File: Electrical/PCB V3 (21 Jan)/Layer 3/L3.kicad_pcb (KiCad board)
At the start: 2 copper layers, 117.9 x 110 mm, 28 parts, among them J1 Conn_01x06, J2 Conn_02x08_Odd_Even, J3 Conn_01x06, J4 Conn_01x06, J5 Conn_01x06, U2 113991054, U3 4754

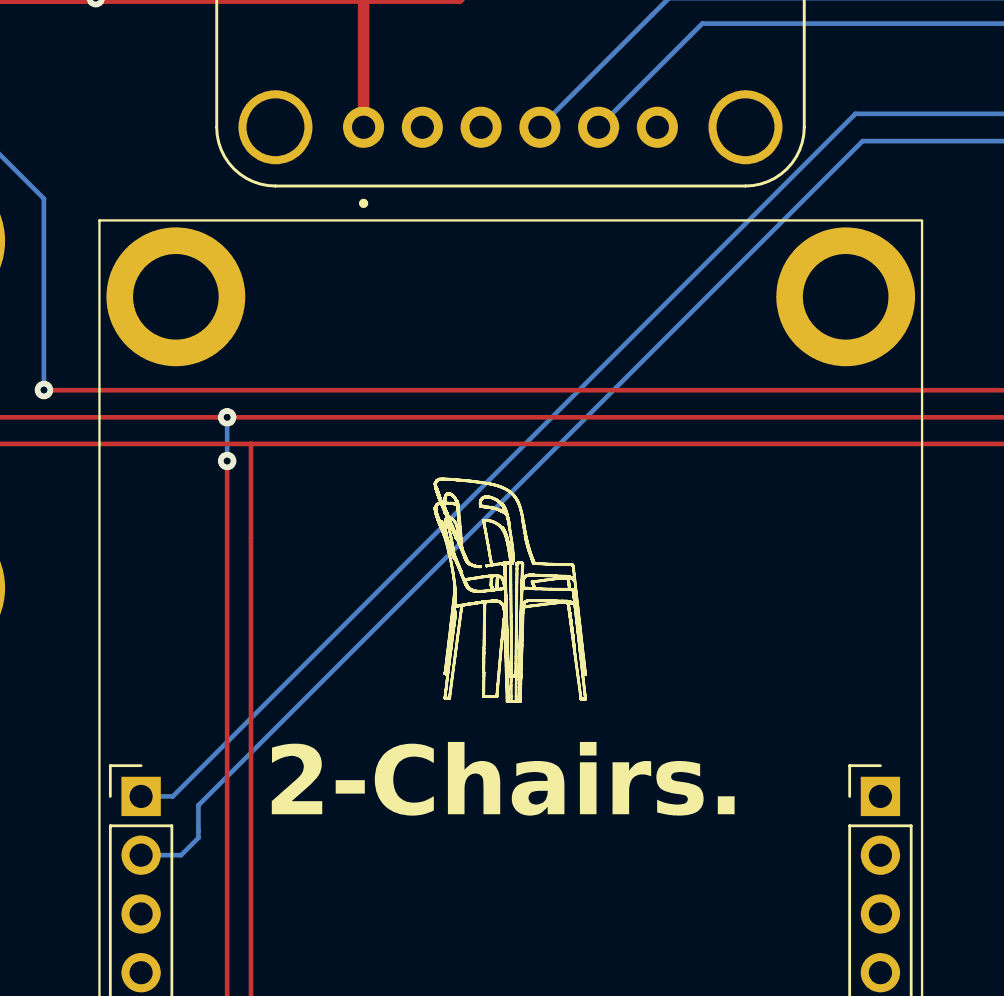
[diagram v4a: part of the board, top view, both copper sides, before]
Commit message: change l3 files to kicad 9, made ONE trace look nicer
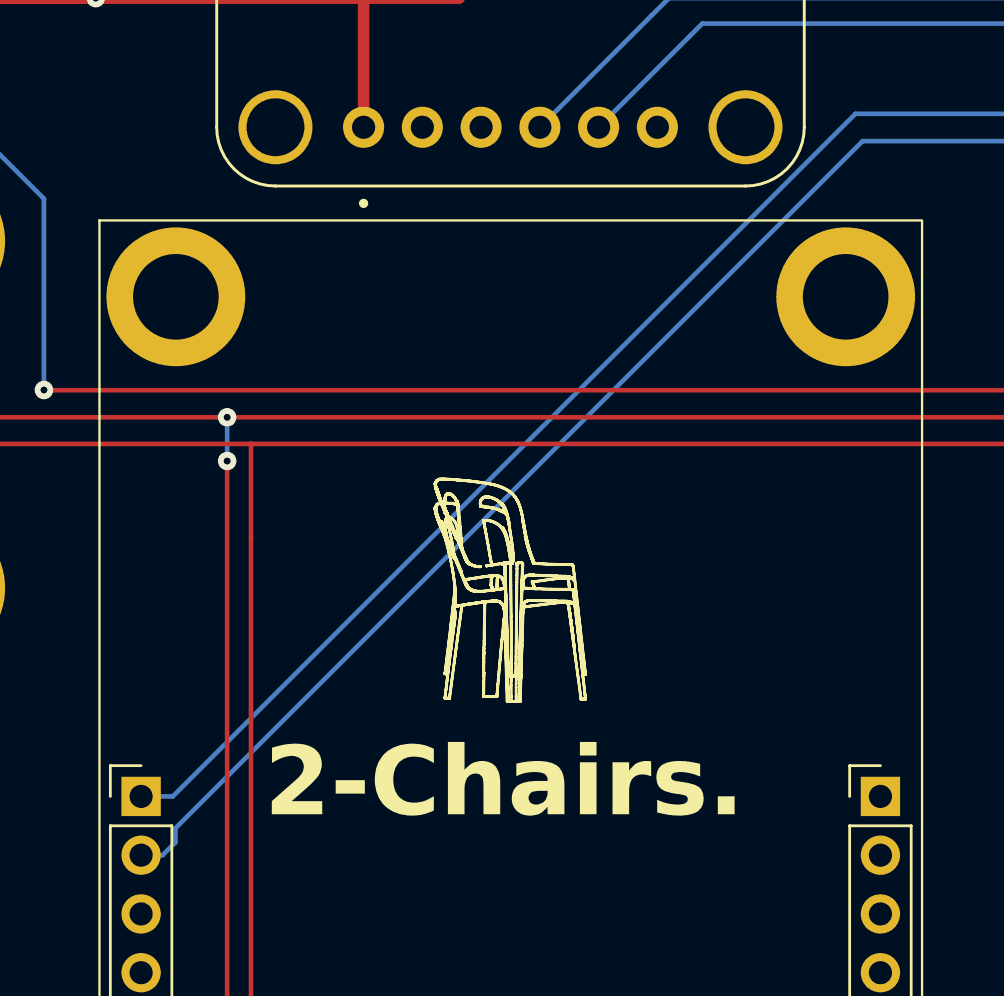
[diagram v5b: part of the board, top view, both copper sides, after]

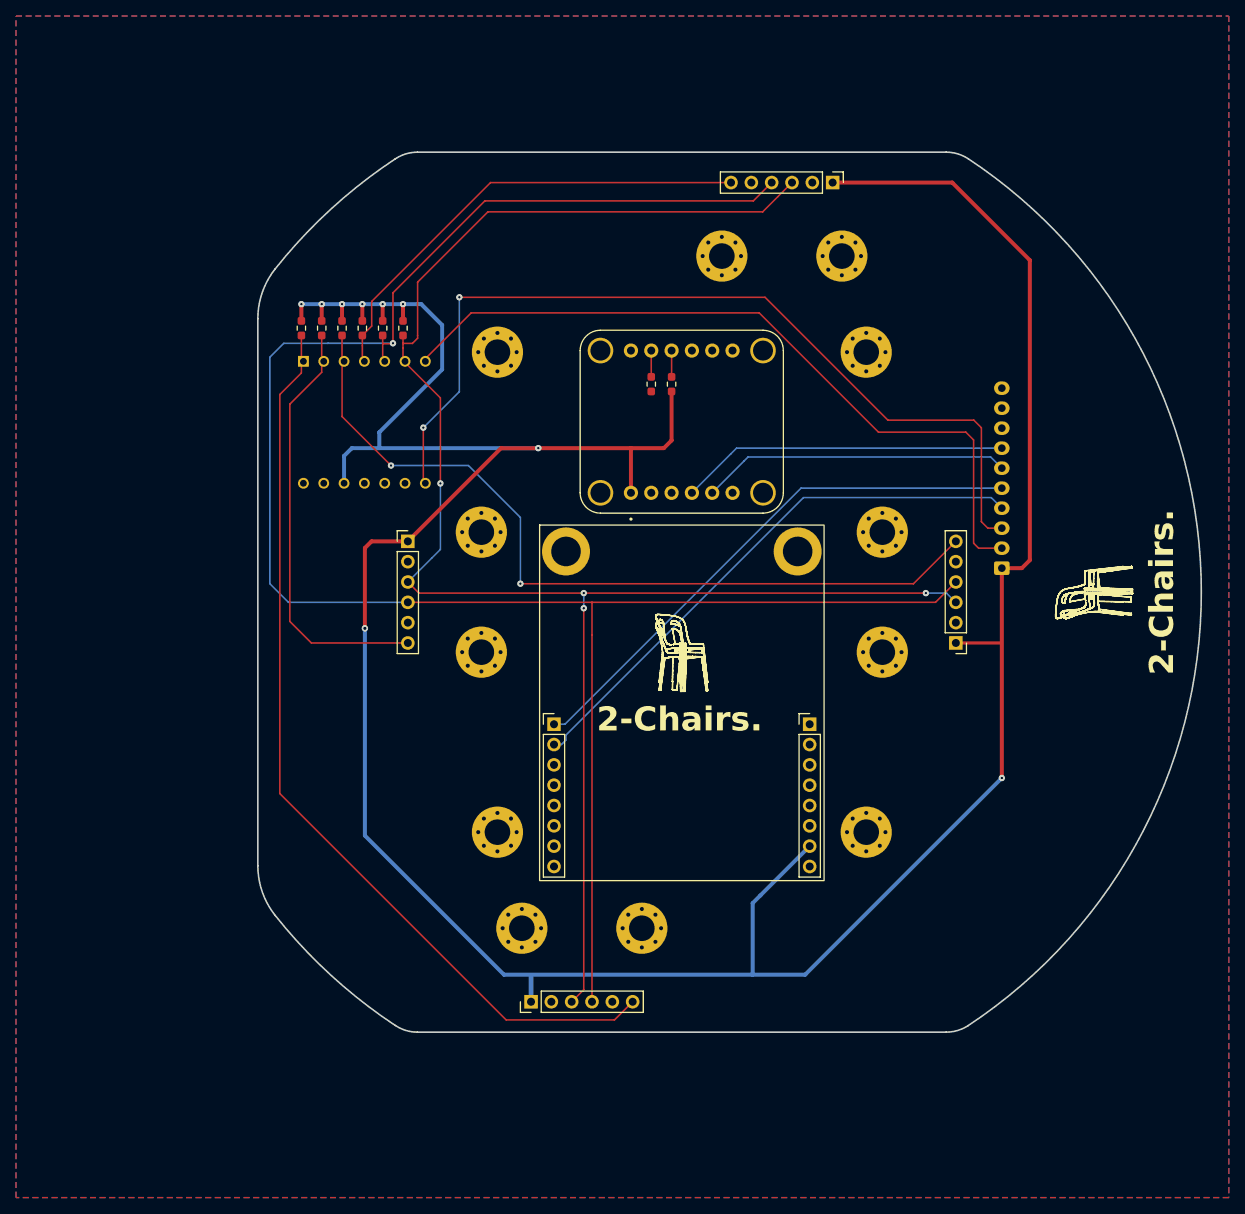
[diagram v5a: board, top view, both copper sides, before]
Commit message: fixed l1 and l3
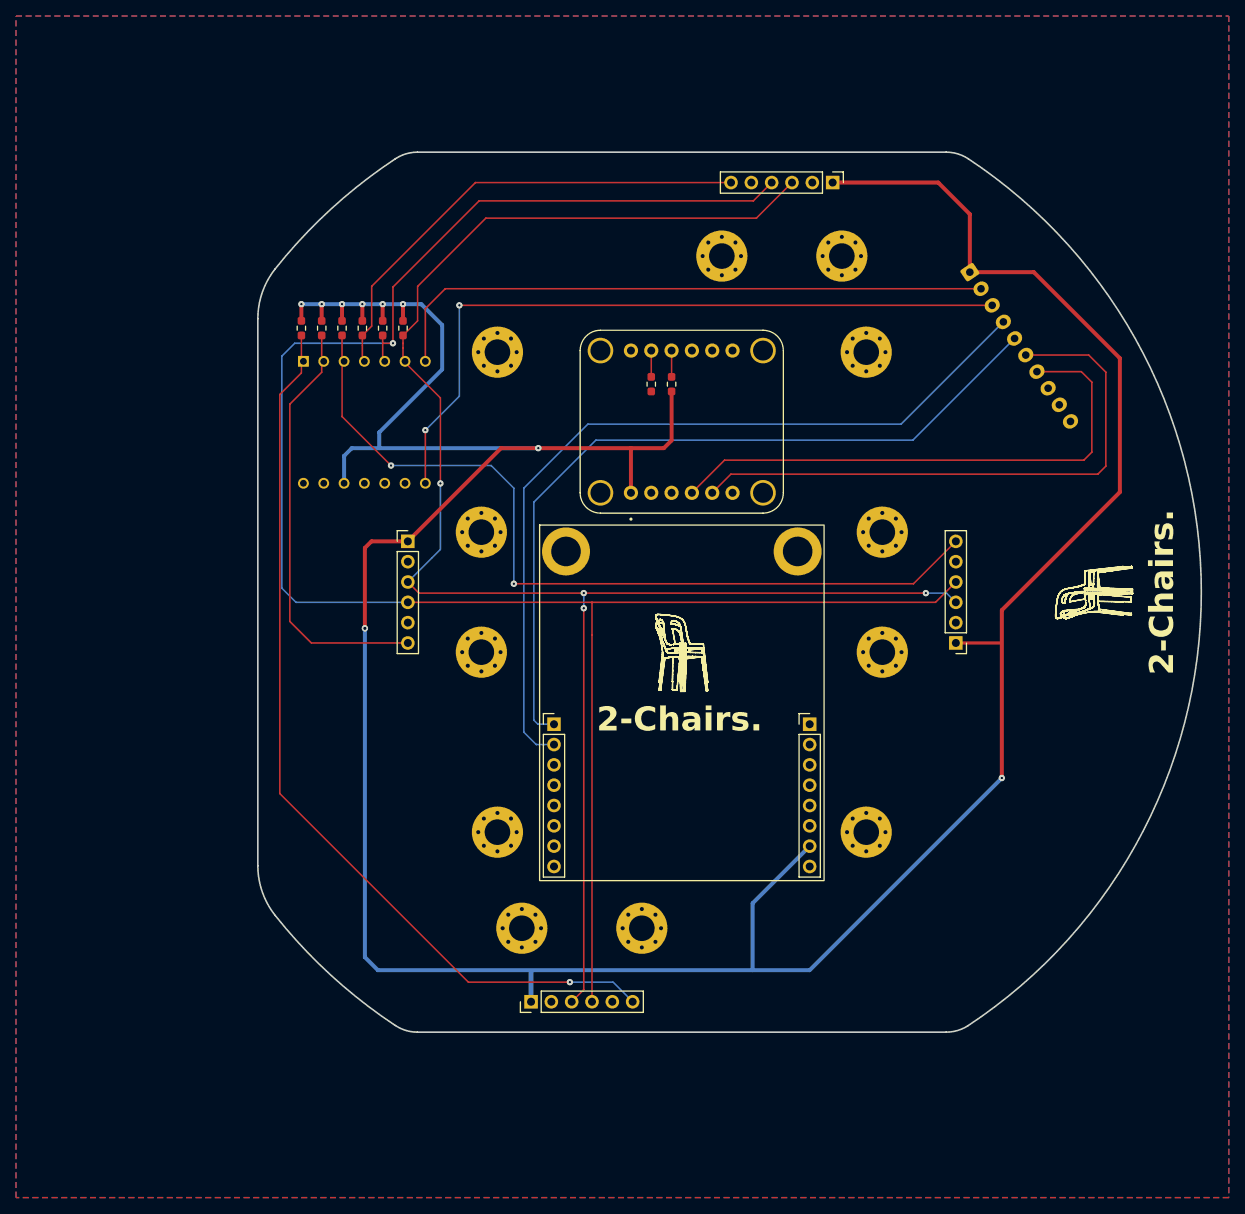
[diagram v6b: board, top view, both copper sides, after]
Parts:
- moved J2 37.2 mm to (249.7, 47.5), turned to -56 degrees
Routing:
- net /TX (IMU): track 38.6 -> 73.2 mm
- net /TX (CAM): track 70.2 -> 104.0 mm
- net /RX (CAM): track 68.2 -> 98.5 mm
- net /RX (IMU): track 41.1 -> 68.3 mm
- net /RX (L3 ESP32): track 111.7 -> 90.6 mm
- net +3V3: track 390.8 -> 410.7 mm
- net /TX (L3 ESP32): track 94.5 -> 77.1 mm
- net /SDA: track 245.9 -> 243.7 mm
- net /TOF3 XSHUT: track 102.6 -> 104.7 mm
- net /SCL: track 216.8 -> 214.8 mm
- net /TOF1 XSHUT: track 115.1 -> 113.3 mm, vias 0 -> 1
- net /TOF4 XSHUT: track 59.0 -> 60.1 mm

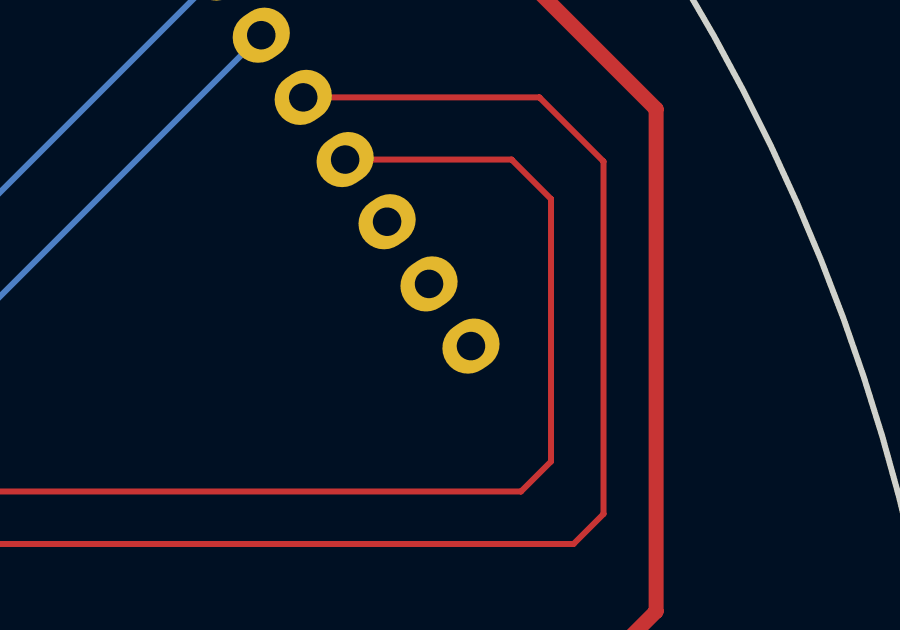
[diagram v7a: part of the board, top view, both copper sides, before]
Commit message: fixed l2, exported new l2 and l3 steps
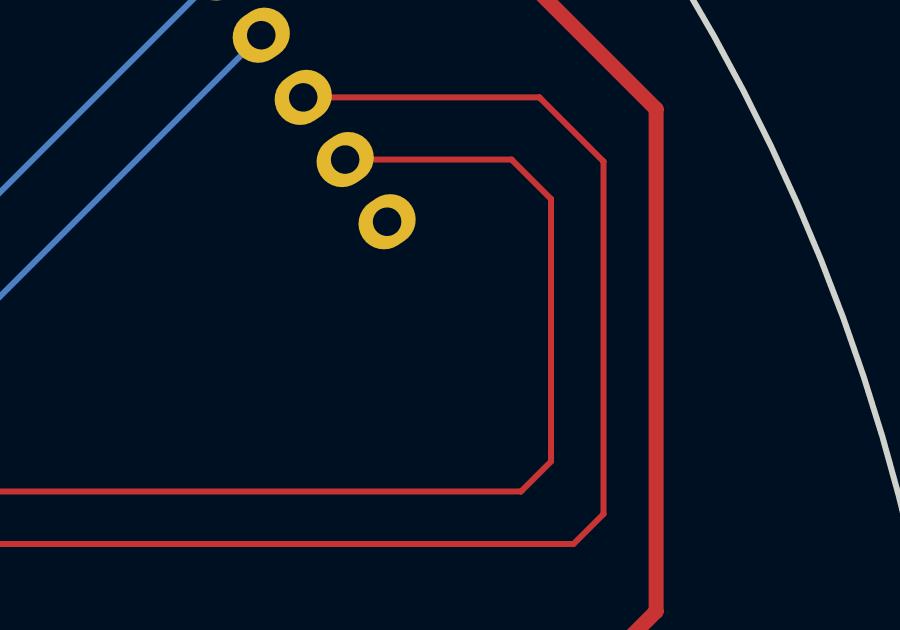
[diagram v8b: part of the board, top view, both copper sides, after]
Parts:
- J2: footprint Connector_JST:JST_XH_B10B-XH-A_1x10_P2.50mm_Vertical -> Connector_JST:JST_XH_B8B-XH-A_1x08_P2.50mm_Vertical
